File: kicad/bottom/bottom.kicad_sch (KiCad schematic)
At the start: 17 parts, among them J1 Conn_01x15_Socket

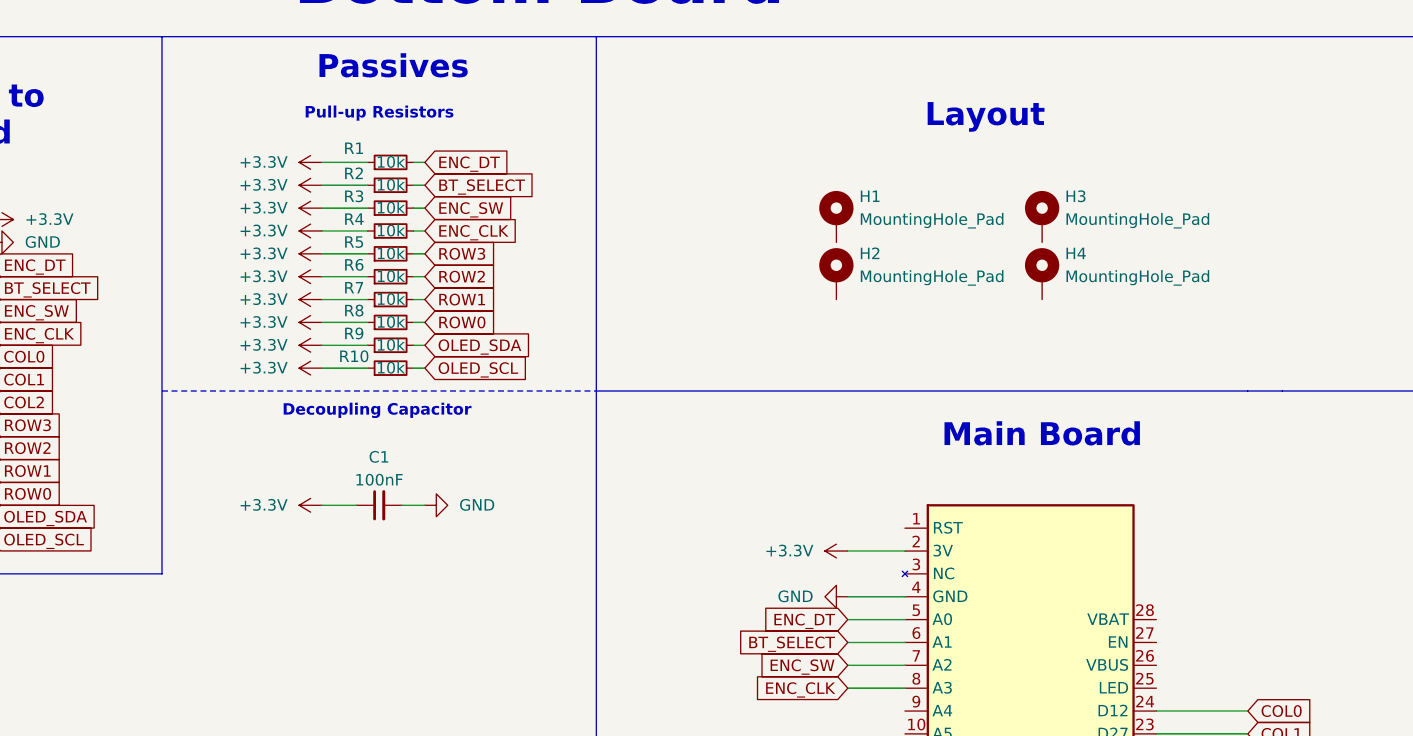
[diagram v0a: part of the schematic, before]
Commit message: delete duplicate top folder, finished wiring on bottom pcb, need better wiring on top pcb
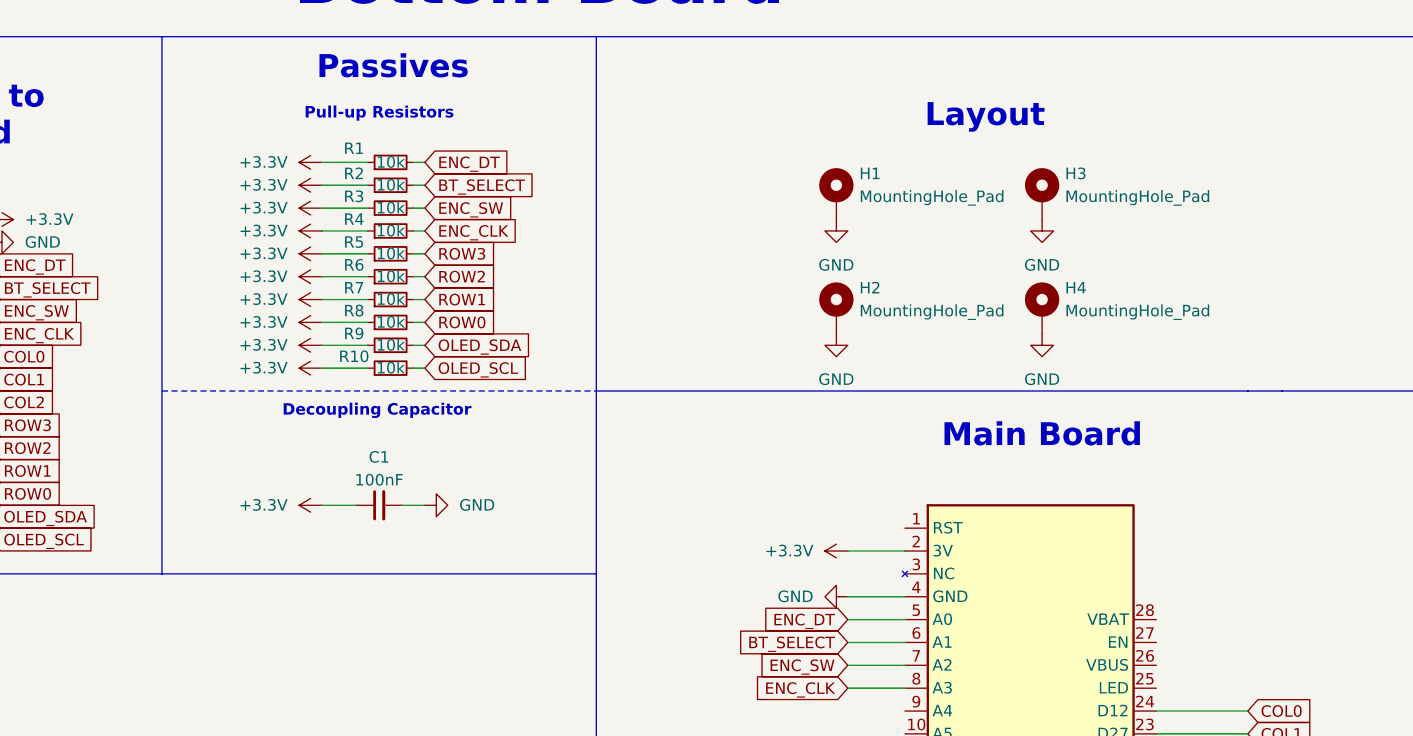
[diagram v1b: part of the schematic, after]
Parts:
- R1, R10, R2, R3, R4, R5, R6, R7, R8, R9: footprint Resistor_SMD:R_1206_3216Metric_Pad1.30x1.75mm_HandSolder -> Resistor_SMD:R_0805_2012Metric_Pad1.20x1.40mm_HandSolder
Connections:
- net GND: now also H1.1, H2.1, H3.1, H4.1
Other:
- moved on the sheet: H1, H2, H3, H4

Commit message: modify paths and file locations for portability, added mounting pins to encoder, changed symbol, footprint and 3d of switch to correlate to what im using
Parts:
- A1: footprint Module:Adafruit_Feather -> Bottom-Footprints:Adafruit_Feather; symbol MCU_Module:Adafruit_Feather_Generic -> Bottom-Symbols:Adafruit_Feather_Generic
- C1: footprint Capacitor_SMD:C_1206_3216Metric_Pad1.33x1.80mm_HandSolder -> Bottom-Footprints:C_1206_3216Metric_Pad1.33x1.80mm_HandSolder; symbol Device:C_Small -> Bottom-Symbols:C_Small
- H1, H2, H3, H4: footprint MountingHole:MountingHole_2.2mm_M2_DIN965_Pad -> Bottom-Footprints:MountingHole_2.2mm_M2_DIN965_Pad; symbol Mechanical:MountingHole_Pad -> Bottom-Symbols:MountingHole_Pad
- J1: footprint Connector_PinSocket_2.54mm:PinSocket_1x15_P2.54mm_Vertical -> Bottom-Footprints:PinSocket_1x15_P2.54mm_Vertical; symbol Connector:Conn_01x15_Socket -> Bottom-Symbols:Conn_01x15_Socket
- R1, R10, R2, R3, R4, R5, R6, R7, R8, R9: footprint Resistor_SMD:R_0805_2012Metric_Pad1.20x1.40mm_HandSolder -> Bottom-Footprints:R_0805_2012Metric_Pad1.20x1.40mm_HandSolder; symbol Device:R_Small -> Bottom-Symbols:R_Small
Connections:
- no-connect marks 0 -> 12
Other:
- moved on the sheet: C1, H1, H2, H3, H4

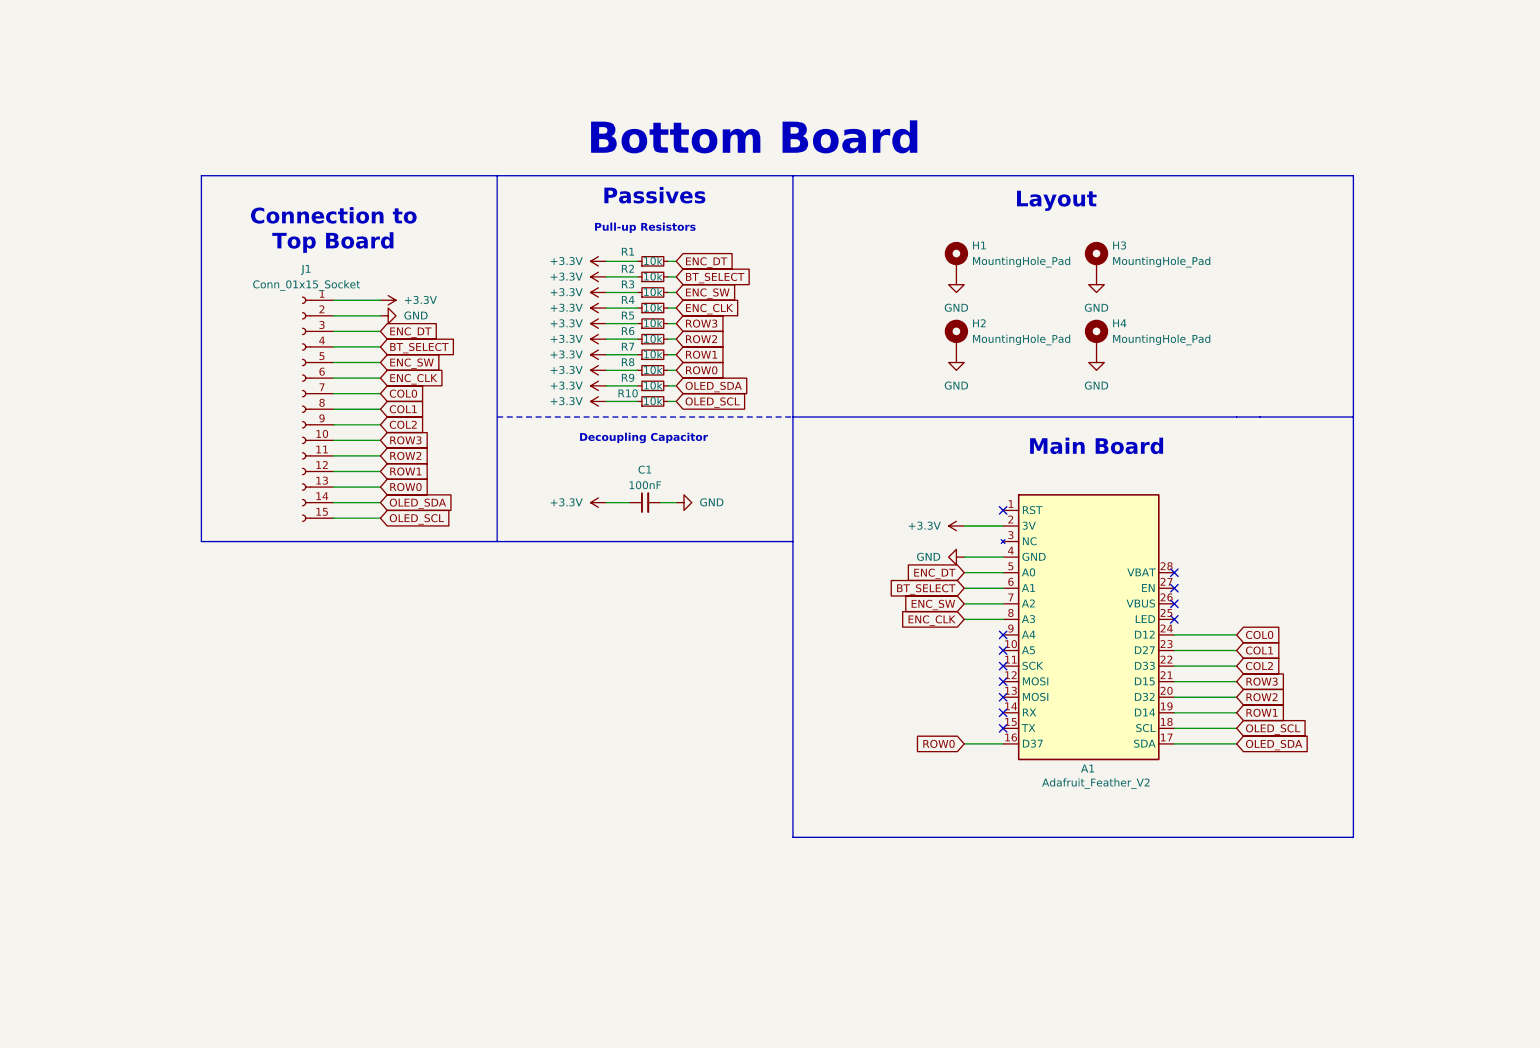
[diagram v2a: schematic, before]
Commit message: finalised mounting hole and pins position, changed gpios
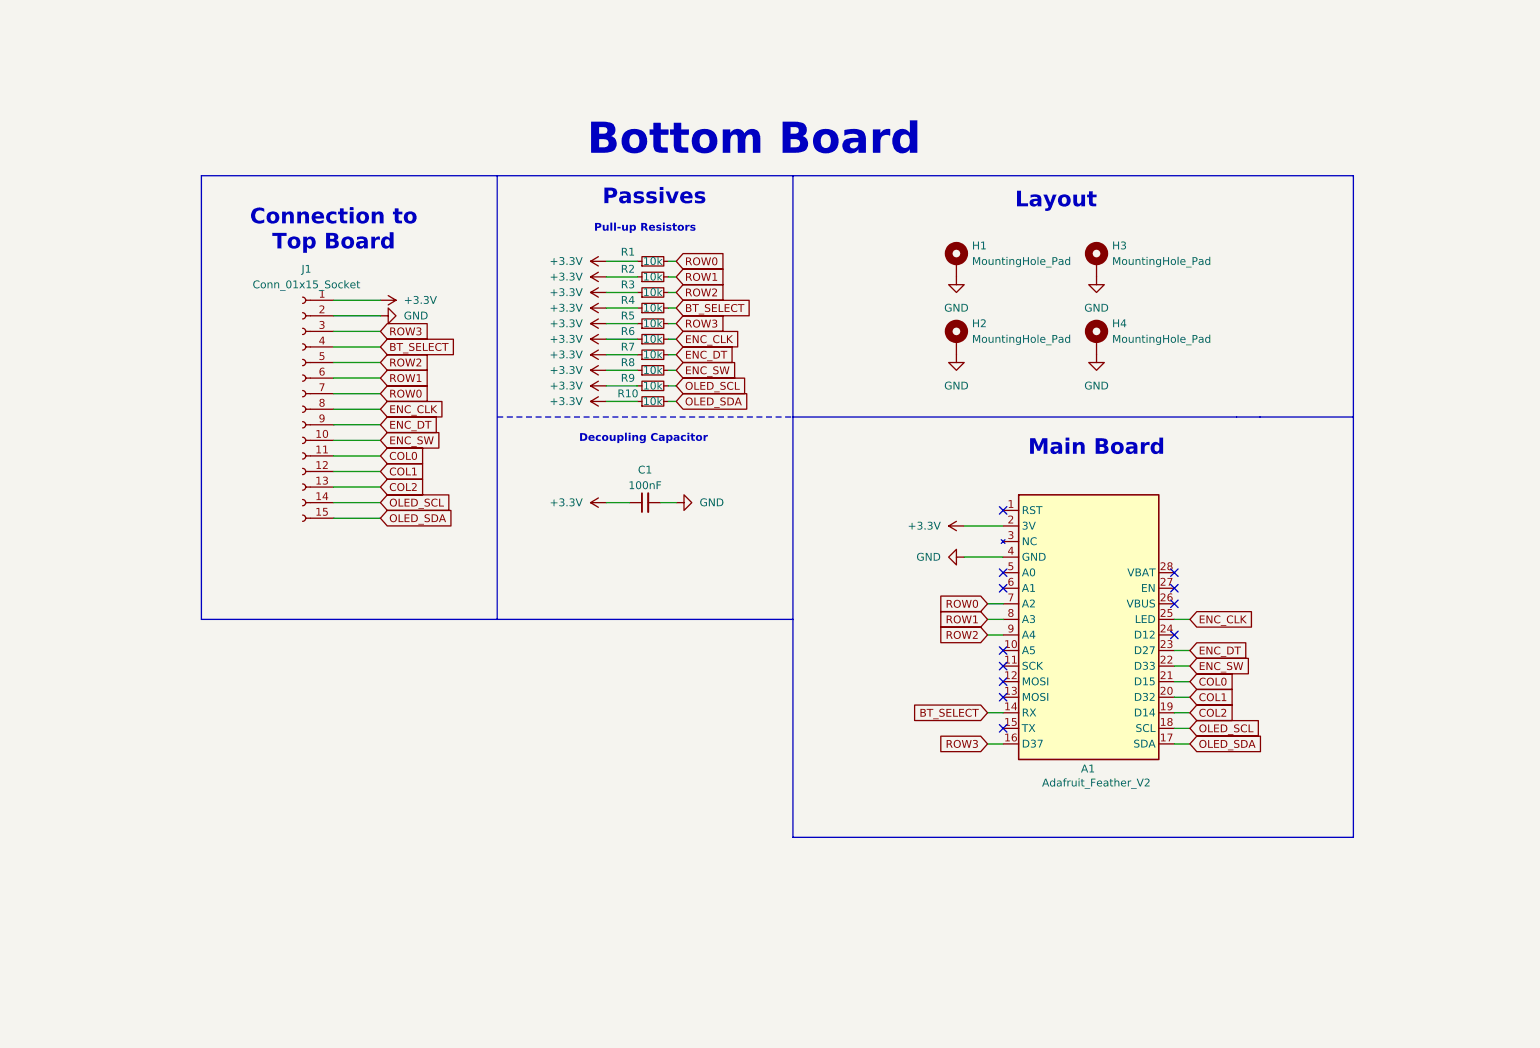
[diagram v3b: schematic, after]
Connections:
- net BT_SELECT: now also A1.14 (RX), R4.2; no longer A1.6 (A1), R2.2
- net COL0: now also A1.21 (D15), J1.11 (Pin_11); no longer A1.24 (D12), J1.7 (Pin_7)
- net COL1: now also A1.20 (D32), J1.12 (Pin_12); no longer A1.23 (D27), J1.8 (Pin_8)
- net COL2: now also A1.19 (D14), J1.13 (Pin_13); no longer A1.22 (D33), J1.9 (Pin_9)
- net ENC_CLK: now also A1.25 (LED), J1.8 (Pin_8), R6.2; no longer A1.8 (A3), J1.6 (Pin_6), R4.2
- net ENC_DT: now also A1.23 (D27), J1.9 (Pin_9), R7.2; no longer A1.5 (A0), J1.3 (Pin_3), R1.2
- net ENC_SW: now also A1.22 (D33), J1.10 (Pin_10), R8.2; no longer A1.7 (A2), J1.5 (Pin_5), R3.2
- net OLED_SCL: now also J1.14 (Pin_14), R9.2; no longer J1.15 (Pin_15), R10.2
- net OLED_SDA: now also J1.15 (Pin_15), R10.2; no longer J1.14 (Pin_14), R9.2
- net ROW0: now also A1.7 (A2), J1.7 (Pin_7), R1.2; no longer A1.16 (D37), J1.13 (Pin_13), R8.2
- net ROW1: now also A1.8 (A3), J1.6 (Pin_6), R2.2; no longer A1.19 (D14), J1.12 (Pin_12), R7.2
- net ROW2: now also A1.9 (A4), J1.5 (Pin_5), R3.2; no longer A1.20 (D32), J1.11 (Pin_11), R6.2
- net ROW3: now also A1.16 (D37), J1.3 (Pin_3); no longer A1.21 (D15), J1.10 (Pin_10)

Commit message: Changed from Adafruit Feather V2 to UnkownMaker ProS3 [D] for USB HID feature. Changed OLED from 128x64 to 128x32
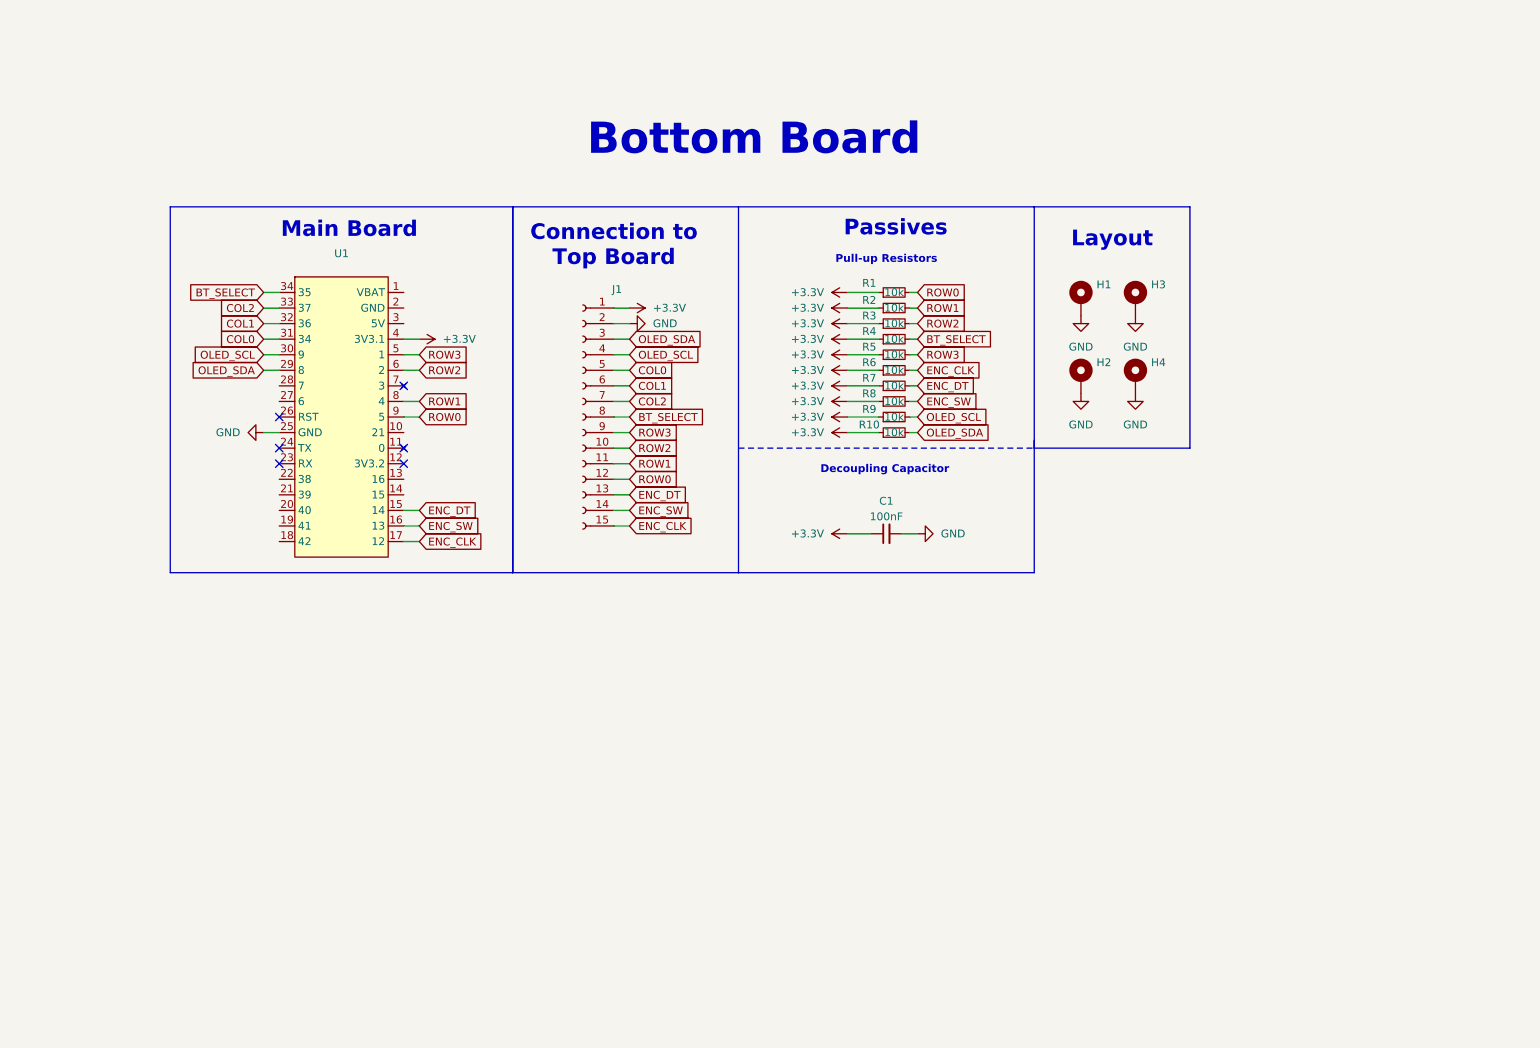
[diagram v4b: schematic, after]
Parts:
- removed A1: Adafruit_Feather_V2, Bottom-Footprints:Adafruit_Feather, symbol Bottom-Symbols:Adafruit_Feather_Generic
- added U1: ~, Bottom-Footprints:ProS3_TH, symbol Bottom-Symbols:ProS3-D
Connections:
- net +3.3V: now also U1.4 (3V3.1)
- net BT_SELECT: now also J1.8 (Pin_8), U1.34 (35); no longer J1.4 (Pin_4)
- net COL0: now also J1.5 (Pin_5), U1.31 (34); no longer J1.11 (Pin_11)
- net COL1: now also J1.6 (Pin_6), U1.32 (36); no longer J1.12 (Pin_12)
- net COL2: now also J1.7 (Pin_7), U1.33 (37); no longer J1.13 (Pin_13)
- net ENC_CLK: now also J1.15 (Pin_15), U1.17 (12); no longer J1.8 (Pin_8)
- net ENC_DT: now also J1.13 (Pin_13), U1.15 (14); no longer J1.9 (Pin_9)
- net ENC_SW: now also J1.14 (Pin_14), U1.16 (13); no longer J1.10 (Pin_10)
- net GND: now also U1.25 (GND)
- net OLED_SCL: now also J1.4 (Pin_4), U1.30 (9); no longer J1.14 (Pin_14)
- net OLED_SDA: now also J1.3 (Pin_3), U1.29 (8); no longer J1.15 (Pin_15)
- net ROW0: now also J1.12 (Pin_12), U1.9 (5); no longer J1.7 (Pin_7)
- net ROW1: now also J1.11 (Pin_11), U1.8 (4); no longer J1.6 (Pin_6)
- net ROW2: now also J1.10 (Pin_10), U1.6 (2); no longer J1.5 (Pin_5)
- net ROW3: now also J1.9 (Pin_9), U1.5 (1); no longer J1.3 (Pin_3)
- no-connect marks 12 -> 6
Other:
- moved on the sheet: C1, H1, H2, H3, H4, J1, R1, R10, R2, R3, R4, R5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

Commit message: added visuals, updated the documentation
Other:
- moved on the sheet: C1, H1, H2, H3, H4, J1, R1, R10, R2, R3, R4, R5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
